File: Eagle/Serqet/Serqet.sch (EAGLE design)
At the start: 47 parts, among them U1 AD9283, U2 AD8330ARQZ, X1 1-227161-0

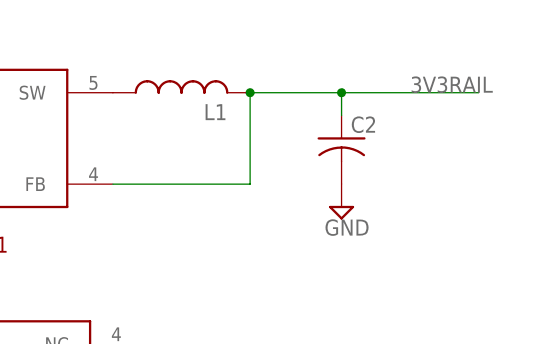
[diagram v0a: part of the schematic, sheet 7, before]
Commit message: Changed 3V3Rail net to Vcc
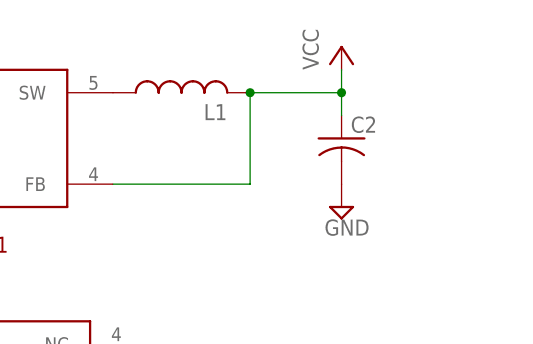
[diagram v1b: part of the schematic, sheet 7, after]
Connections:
- removed net 3V3RAIL: C2.1, L1.2, U$2.FB
- net VCC: now also C2.1, L1.2, U$2.FB
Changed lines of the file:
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@@
 <part name="P+10" library="supply1" deviceset="VCC" device=""/>
 <part name="SUPPLY19" library="supply2" deviceset="GND" device=""/>
+<part name="P+11" library="supply1" deviceset="VCC" device=""/>
 </parts>
 <sheets>
@@
 <instance part="U$6" gate="G$1" x="-2.54" y="63.5"/>
 <instance part="SUPPLY12" gate="GND" x="5.08" y="48.26"/>
+<instance part="P+11" gate="VCC" x="99.06" y="71.12"/>
 </instances>
 <busses>
@@
 </segment>
 </net>
-<net name="3V3RAIL" class="0">
+<net name="5VRAIL" class="0">
+<segment>
+<pinref part="DCDCBOOST1" gate="G$1" pin="+VOUT"/>
+<wire x1="76.2" y1="30.48" x2="96.52" y2="30.48" width="0.1524" layer="91"/>
+<label x="91.44" y="30.48" size="1.778" layer="95"/>
+</segment>
+</net>
+<net name="VCC" class="0">
 <segment>
 <pinref part="U$2" gate="G$1" pin="FB"/>
@@
 <wire x1="99.06" y1="66.04" x2="99.06" y2="63.5" width="0.1524" layer="91"/>
 <junction x="88.9" y="66.04"/>
-<wire x1="99.06" y1="66.04" x2="114.3" y2="66.04" width="0.1524" layer="91"/>
 <junction x="99.06" y="66.04"/>
-<label x="106.68" y="66.04" size="1.778" layer="95"/>
-</segment>
-</net>
-<net name="5VRAIL" class="0">
-<segment>
-<pinref part="DCDCBOOST1" gate="G$1" pin="+VOUT"/>
-<wire x1="76.2" y1="30.48" x2="96.52" y2="30.48" width="0.1524" layer="91"/>
-<label x="91.44" y="30.48" size="1.778" layer="95"/>
-</segment>
-</net>
+<pinref part="P+11" gate="VCC" pin="VCC"/>
+<wire x1="99.06" y1="68.58" x2="99.06" y2="66.04" width="0.1524" layer="91"/>
+</segment>
+</net>

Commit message: Added bus to ADC out
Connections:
- new net ADC_OUT_0: U1.D0
- new net ADC_OUT_1: U1.D1
- new net ADC_OUT_2: U1.D2
- new net ADC_OUT_3: U1.D3
- new net ADC_OUT_4: U1.D4
- new net ADC_OUT_5: U1.D5
- new net ADC_OUT_6: U1.D6
- new net ADC_OUT_7: U1.D7
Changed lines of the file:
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@@
 </instances>
 <busses>
+<bus name="ADC_OUT_[0..7]">
+<segment>
+<wire x1="81.28" y1="48.26" x2="81.28" y2="68.58" width="0.762" layer="92"/>
+<wire x1="81.28" y1="68.58" x2="91.44" y2="68.58" width="0.762" layer="92"/>
+<label x="81.28" y="71.12" size="1.778" layer="95"/>
+</segment>
+</bus>
 </busses>
 <nets>
@@
 </segment>
 </net>
+<net name="ADC_OUT_0" class="0">
+<segment>
+<pinref part="U1" gate="U" pin="D0"/>
+<wire x1="81.28" y1="48.26" x2="71.12" y2="48.26" width="0.1524" layer="91"/>
+</segment>
+</net>
+<net name="ADC_OUT_1" class="0">
+<segment>
+<pinref part="U1" gate="U" pin="D1"/>
+<wire x1="81.28" y1="50.8" x2="71.12" y2="50.8" width="0.1524" layer="91"/>
+</segment>
+</net>
+<net name="ADC_OUT_2" class="0">
+<segment>
+<pinref part="U1" gate="U" pin="D2"/>
+<wire x1="81.28" y1="53.34" x2="71.12" y2="53.34" width="0.1524" layer="91"/>
+</segment>
+</net>
+<net name="ADC_OUT_3" class="0">
+<segment>
+<pinref part="U1" gate="U" pin="D3"/>
+<wire x1="81.28" y1="55.88" x2="71.12" y2="55.88" width="0.1524" layer="91"/>
+</segment>
+</net>
+<net name="ADC_OUT_4" class="0">
+<segment>
+<pinref part="U1" gate="U" pin="D4"/>
+<wire x1="81.28" y1="58.42" x2="71.12" y2="58.42" width="0.1524" layer="91"/>
+</segment>
+</net>
+<net name="ADC_OUT_5" class="0">
+<segment>
+<pinref part="U1" gate="U" pin="D5"/>
+<wire x1="81.28" y1="60.96" x2="71.12" y2="60.96" width="0.1524" layer="91"/>
+</segment>
+</net>
+<net name="ADC_OUT_6" class="0">
+<segment>
+<pinref part="U1" gate="U" pin="D6"/>
+<wire x1="81.28" y1="63.5" x2="71.12" y2="63.5" width="0.1524" layer="91"/>
+</segment>
+</net>
+<net name="ADC_OUT_7" class="0">
+<segment>
+<pinref part="U1" gate="U" pin="D7"/>
+<wire x1="81.28" y1="66.04" x2="71.12" y2="66.04" width="0.1524" layer="91"/>
+</segment>
+</net>

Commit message: Added FPGA to sheet
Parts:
- added KNJN_FPGA1: KNJNRS232FPGAPLUTO-IIKNJNRS232FPGAPLUTO-II, KNJN_RS232_FPGA_Pluto-II:KNJNRS232FPGAPLUTO-IIKNJNRS232FPGAPLUTO-II
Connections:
- net ADC_ENCODE: now also KNJN_FPGA1.ADC_ENCODE
- net ADC_OUT_0: now also KNJN_FPGA1.ADC_OUT_0
- net ADC_OUT_1: now also KNJN_FPGA1.ADC_OUT_1
- net ADC_OUT_2: now also KNJN_FPGA1.ADC_OUT_2
- net ADC_OUT_3: now also KNJN_FPGA1.ADC_OUT_3
- net ADC_OUT_4: now also KNJN_FPGA1.ADC_OUT_4
- net ADC_OUT_5: now also KNJN_FPGA1.ADC_OUT_5
- net ADC_OUT_6: now also KNJN_FPGA1.ADC_OUT_6
- net ADC_OUT_7: now also KNJN_FPGA1.ADC_OUT_7
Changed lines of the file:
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@@
 <part name="SUPPLY19" library="supply2" deviceset="GND" device=""/>
 <part name="P+11" library="supply1" deviceset="VCC" device=""/>
+<part name="KNJN_FPGA1" library="KNJN_RS232_FPGA_Pluto-II" deviceset="KNJNRS232FPGAPLUTO-II" device="KNJNRS232FPGAPLUTO-II"/>
 </parts>
 <sheets>
@@
 </plain>
 <instances>
-</instances>
-<busses>
-</busses>
-<nets>
-</nets>
-</sheet>
+<instance part="KNJN_FPGA1" gate="G$1" x="66.04" y="66.04"/>
+</instances>
+<busses>
+<bus name="ADC_OUT_[0..7]">
+<segment>
+<wire x1="0" y1="91.44" x2="10.16" y2="91.44" width="0.762" layer="92"/>
+<wire x1="10.16" y1="91.44" x2="10.16" y2="68.58" width="0.762" layer="92"/>
+<label x="0" y="93.98" size="1.778" layer="95"/>
+</segment>
+</bus>
+</busses>
+<nets>
+<net name="ADC_OUT_0" class="0">
+<segment>
+<pinref part="KNJN_FPGA1" gate="G$1" pin="ADC_OUT_0"/>
+<wire x1="22.86" y1="86.36" x2="10.16" y2="86.36" width="0.1524" layer="91"/>
+</segment>
+</net>
+<net name="ADC_OUT_1" class="0">
+<segment>
+<pinref part="KNJN_FPGA1" gate="G$1" pin="ADC_OUT_1"/>
+<wire x1="22.86" y1="83.82" x2="10.16" y2="83.82" width="0.1524" layer="91"/>
+</segment>
+</net>
+<net name="ADC_OUT_2" class="0">
+<segment>
+<pinref part="KNJN_FPGA1" gate="G$1" pin="ADC_OUT_2"/>
+<wire x1="22.86" y1="81.28" x2="10.16" y2="81.28" width="0.1524" layer="91"/>
+</segment>
+</net>
+<net name="ADC_OUT_4" class="0">
+<segment>
+<pinref part="KNJN_FPGA1" gate="G$1" pin="ADC_OUT_4"/>
+<wire x1="22.86" y1="76.2" x2="10.16" y2="76.2" width="0.1524" layer="91"/>
+</segment>
+</net>
+<net name="ADC_OUT_5" class="0">
+<segment>
+<pinref part="KNJN_FPGA1" gate="G$1" pin="ADC_OUT_5"/>
+<wire x1="22.86" y1="73.66" x2="10.16" y2="73.66" width="0.1524" layer="91"/>
+</segment>
+</net>
+<net name="ADC_OUT_6" class="0">
+<segment>
+<pinref part="KNJN_FPGA1" gate="G$1" pin="ADC_OUT_6"/>
+<wire x1="22.86" y1="71.12" x2="10.16" y2="71.12" width="0.1524" layer="91"/>
+</segment>
+</net>
+<net name="ADC_OUT_7" class="0">
+<segment>
+<pinref part="KNJN_FPGA1" gate="G$1" pin="ADC_OUT_7"/>
+<wire x1="22.86" y1="68.58" x2="10.16" y2="68.58" width="0.1524" layer="91"/>
+</segment>
+</net>
+<net name="ADC_OUT_3" class="0">
+<segment>
+<pinref part="KNJN_FPGA1" gate="G$1" pin="ADC_OUT_3"/>
+<wire x1="22.86" y1="78.74" x2="10.16" y2="78.74" width="0.1524" layer="91"/>
+</segment>
+</net>
+<net name="ADC_ENCODE" class="0">
+<segment>
+<pinref part="KNJN_FPGA1" gate="G$1" pin="ADC_ENCODE"/>
+<wire x1="22.86" y1="63.5" x2="-2.54" y2="63.5" width="0.1524" layer="91"/>
+<label x="-2.54" y="63.5" size="1.778" layer="95"/>
+</segment>
+</net>
+</nets>
+</sheet>

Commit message: Completed FPGA sheet
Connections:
- net 5VRAIL: now also KNJN_FPGA1.VCC_UNREG
- net GND: now also KNJN_FPGA1.GND, KNJN_FPGA1.GND_1, KNJN_FPGA1.GND_2, KNJN_FPGA1.GND_3, KNJN_FPGA1.GND_4, KNJN_FPGA1.GND_5, KNJN_FPGA1.GND_6
- net VCC: now also KNJN_FPGA1.+3.3V, KNJN_FPGA1.+3.3V_1, KNJN_FPGA1.+3.3V_2, KNJN_FPGA1.+3.3V_3
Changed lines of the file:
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@@
 <part name="P+11" library="supply1" deviceset="VCC" device=""/>
 <part name="KNJN_FPGA1" library="KNJN_RS232_FPGA_Pluto-II" deviceset="KNJNRS232FPGAPLUTO-II" device="KNJNRS232FPGAPLUTO-II"/>
+<part name="P+12" library="supply1" deviceset="VCC" device=""/>
+<part name="SUPPLY20" library="supply2" deviceset="GND" device=""/>
 </parts>
 <sheets>
@@
 <instances>
 <instance part="KNJN_FPGA1" gate="G$1" x="66.04" y="66.04"/>
+<instance part="P+12" gate="VCC" x="-15.24" y="40.64"/>
+<instance part="SUPPLY20" gate="GND" x="-25.4" y="40.64"/>
 </instances>
 <busses>
@@
 </segment>
 </net>
+<net name="5VRAIL" class="0">
+<segment>
+<pinref part="KNJN_FPGA1" gate="G$1" pin="VCC_UNREG"/>
+<wire x1="22.86" y1="17.78" x2="10.16" y2="17.78" width="0.1524" layer="91"/>
+<label x="0" y="17.78" size="1.778" layer="95"/>
+</segment>
+</net>
+<net name="VCC" class="0">
+<segment>
+<pinref part="KNJN_FPGA1" gate="G$1" pin="+3.3V"/>
+<wire x1="22.86" y1="30.48" x2="15.24" y2="30.48" width="0.1524" layer="91"/>
+<wire x1="15.24" y1="30.48" x2="15.24" y2="27.94" width="0.1524" layer="91"/>
+<pinref part="KNJN_FPGA1" gate="G$1" pin="+3.3V_1"/>
+<wire x1="15.24" y1="27.94" x2="22.86" y2="27.94" width="0.1524" layer="91"/>
+<wire x1="15.24" y1="27.94" x2="15.24" y2="25.4" width="0.1524" layer="91"/>
+<junction x="15.24" y="27.94"/>
+<pinref part="KNJN_FPGA1" gate="G$1" pin="+3.3V_2"/>
+<wire x1="15.24" y1="25.4" x2="22.86" y2="25.4" width="0.1524" layer="91"/>
+<wire x1="15.24" y1="25.4" x2="15.24" y2="22.86" width="0.1524" layer="91"/>
+<junction x="15.24" y="25.4"/>
+<pinref part="KNJN_FPGA1" gate="G$1" pin="+3.3V_3"/>
+<wire x1="15.24" y1="22.86" x2="22.86" y2="22.86" width="0.1524" layer="91"/>
+<junction x="15.24" y="30.48"/>
+<pinref part="P+12" gate="VCC" pin="VCC"/>
+<wire x1="15.24" y1="30.48" x2="-15.24" y2="30.48" width="0.1524" layer="91"/>
+<wire x1="-15.24" y1="30.48" x2="-15.24" y2="38.1" width="0.1524" layer="91"/>
+</segment>
+</net>
+<net name="GND" class="0">
+<segment>
+<pinref part="SUPPLY20" gate="GND" pin="GND"/>
+<wire x1="-25.4" y1="43.18" x2="-25.4" y2="48.26" width="0.1524" layer="91"/>
+<pinref part="KNJN_FPGA1" gate="G$1" pin="GND_6"/>
+<wire x1="22.86" y1="33.02" x2="15.24" y2="33.02" width="0.1524" layer="91"/>
+<wire x1="15.24" y1="33.02" x2="15.24" y2="35.56" width="0.1524" layer="91"/>
+<pinref part="KNJN_FPGA1" gate="G$1" pin="GND_5"/>
+<wire x1="15.24" y1="35.56" x2="22.86" y2="35.56" width="0.1524" layer="91"/>
+<pinref part="KNJN_FPGA1" gate="G$1" pin="GND_4"/>
+<wire x1="22.86" y1="38.1" x2="15.24" y2="38.1" width="0.1524" layer="91"/>
+<wire x1="15.24" y1="38.1" x2="15.24" y2="35.56" width="0.1524" layer="91"/>
+<junction x="15.24" y="35.56"/>
+<wire x1="15.24" y1="38.1" x2="15.24" y2="40.64" width="0.1524" layer="91"/>
+<junction x="15.24" y="38.1"/>
+<pinref part="KNJN_FPGA1" gate="G$1" pin="GND_3"/>
+<wire x1="22.86" y1="40.64" x2="15.24" y2="40.64" width="0.1524" layer="91"/>
+<wire x1="15.24" y1="40.64" x2="15.24" y2="43.18" width="0.1524" layer="91"/>
+<junction x="15.24" y="40.64"/>
+<pinref part="KNJN_FPGA1" gate="G$1" pin="GND_2"/>
+<wire x1="15.24" y1="43.18" x2="22.86" y2="43.18" width="0.1524" layer="91"/>
+<wire x1="15.24" y1="43.18" x2="15.24" y2="45.72" width="0.1524" layer="91"/>
+<junction x="15.24" y="43.18"/>
+<pinref part="KNJN_FPGA1" gate="G$1" pin="GND_1"/>
+<wire x1="22.86" y1="45.72" x2="15.24" y2="45.72" width="0.1524" layer="91"/>
+<wire x1="15.24" y1="45.72" x2="15.24" y2="48.26" width="0.1524" layer="91"/>
+<junction x="15.24" y="45.72"/>
+<pinref part="KNJN_FPGA1" gate="G$1" pin="GND"/>
+<wire x1="15.24" y1="48.26" x2="22.86" y2="48.26" width="0.1524" layer="91"/>
+<wire x1="15.24" y1="48.26" x2="-25.4" y2="48.26" width="0.1524" layer="91"/>
+<junction x="15.24" y="48.26"/>
+</segment>
+</net>
